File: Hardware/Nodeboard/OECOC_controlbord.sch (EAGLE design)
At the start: 13 parts, among them IC1 DS2405, IC2 DS2405, U1 ESP32-DEVKITC-32D

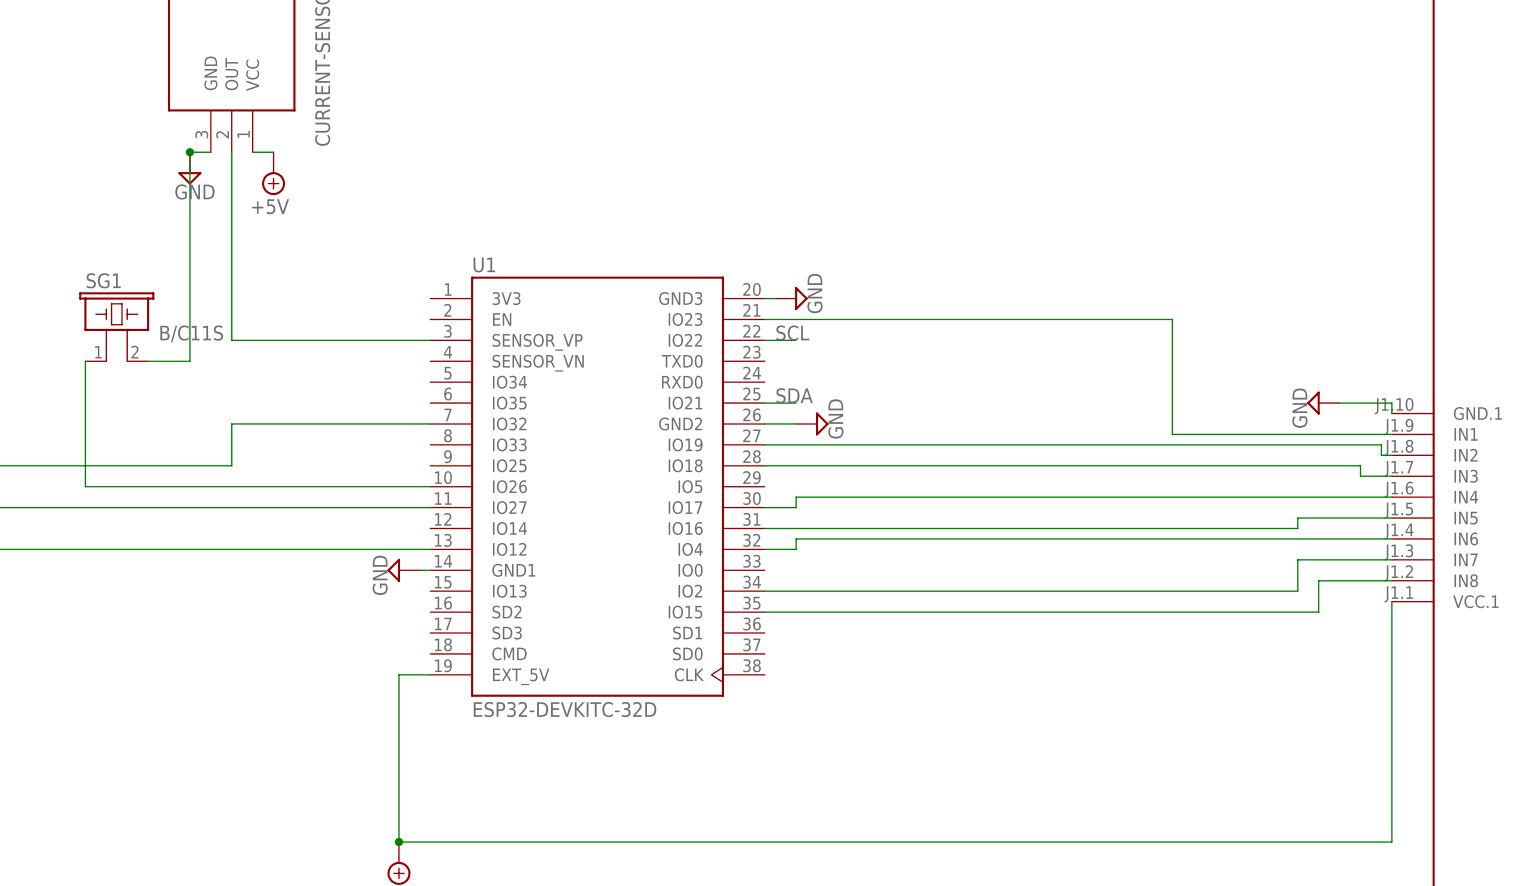
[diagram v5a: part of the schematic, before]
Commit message: changed pins relay
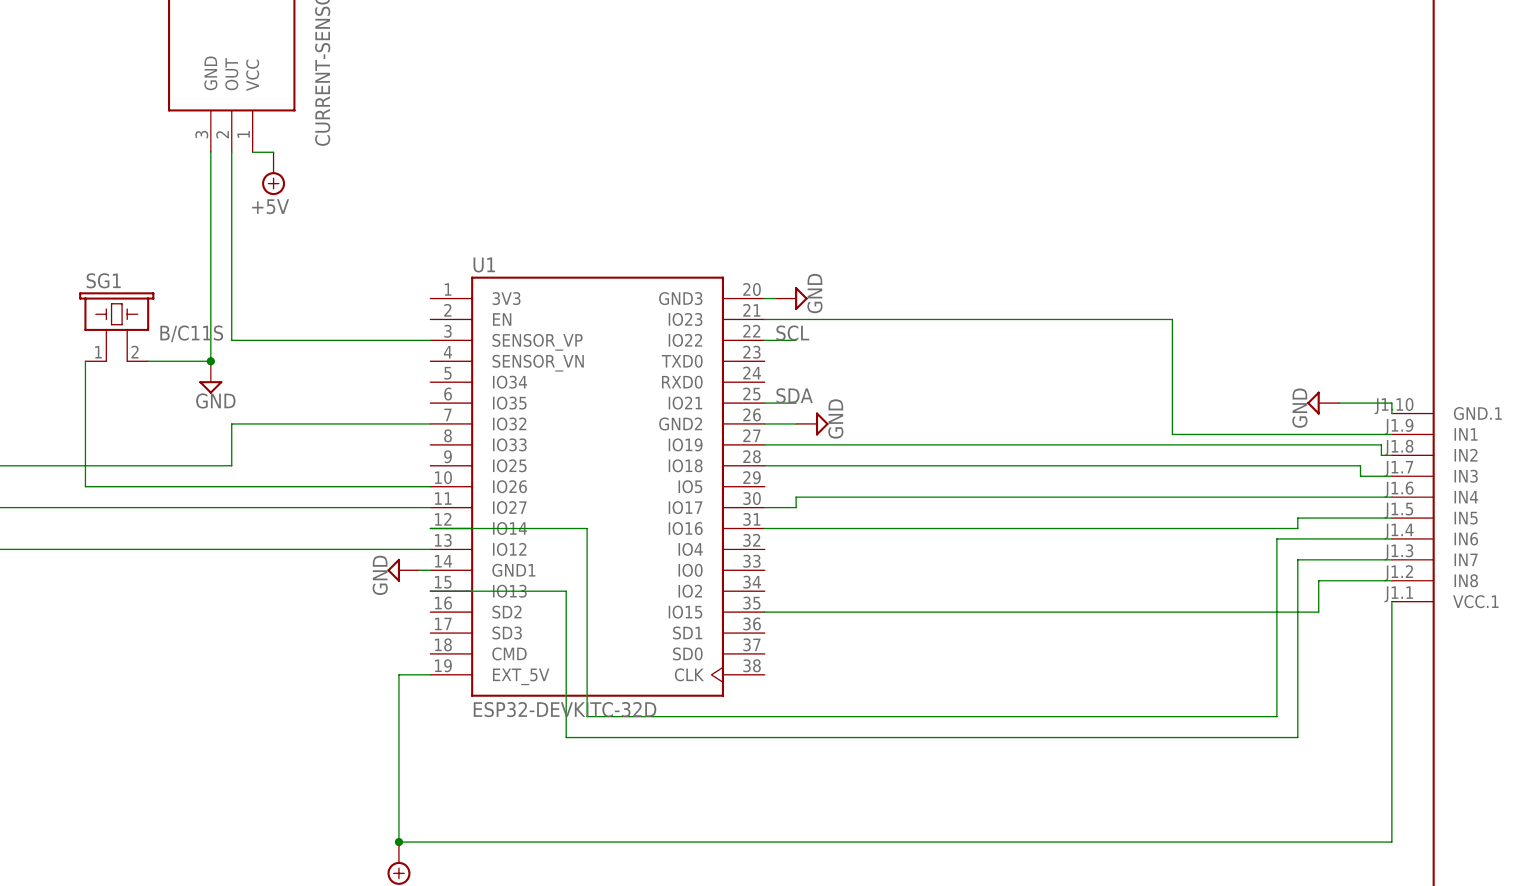
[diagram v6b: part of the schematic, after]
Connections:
- net N$2: now also U1.IO14; no longer U1.IO4
- net N$7: now also U1.IO13; no longer U1.IO2
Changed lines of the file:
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@@
 <attribute name="VALUE" x="194.945" y="210.185" size="1.778" layer="96" rot="R180"/>
 </instance>
-<instance part="G5" gate="G$1" x="182.88" y="213.36" smashed="yes">
-<attribute name="VALUE" x="180.975" y="210.185" size="1.778" layer="96"/>
+<instance part="G5" gate="G$1" x="185.42" y="187.96" smashed="yes">
+<attribute name="VALUE" x="183.515" y="184.785" size="1.778" layer="96"/>
 </instance>
 <instance part="U$5" gate="G$1" x="91.44" y="116.84" smashed="yes" rot="R180">
@@
 <pinref part="G5" gate="G$1" pin="GND"/>
 <pinref part="U$4" gate="G$1" pin="GND"/>
-<wire x1="182.88" y1="215.9" x2="185.42" y2="215.9" width="0.1524" layer="91"/>
+<wire x1="185.42" y1="190.5" x2="185.42" y2="215.9" width="0.1524" layer="91"/>
 <pinref part="SG1" gate="G$1" pin="2"/>
-<wire x1="177.8" y1="190.5" x2="182.88" y2="190.5" width="0.1524" layer="91"/>
-<wire x1="182.88" y1="190.5" x2="182.88" y2="215.9" width="0.1524" layer="91"/>
-<junction x="182.88" y="215.9"/>
+<wire x1="177.8" y1="190.5" x2="185.42" y2="190.5" width="0.1524" layer="91"/>
+<junction x="185.42" y="190.5"/>
 </segment>
 <segment>
@@
 </segment>
 </net>
-<net name="N$2" class="0">
-<segment>
-<pinref part="U1" gate="G$1" pin="IO4"/>
-<wire x1="252.73" y1="167.64" x2="256.54" y2="167.64" width="0.1524" layer="91"/>
-<pinref part="U$1" gate="G$1" pin="IN6"/>
-<wire x1="256.54" y1="167.64" x2="256.54" y2="168.91" width="0.1524" layer="91"/>
-<wire x1="256.54" y1="168.91" x2="328.93" y2="168.91" width="0.1524" layer="91"/>
-</segment>
-</net>
 <net name="N$3" class="0">
 <segment>
@@
 <net name="N$7" class="0">
 <segment>
-<pinref part="U1" gate="G$1" pin="IO2"/>
-<wire x1="252.73" y1="162.56" x2="317.5" y2="162.56" width="0.1524" layer="91"/>
 <pinref part="U$1" gate="G$1" pin="IN7"/>
-<wire x1="317.5" y1="162.56" x2="317.5" y2="166.37" width="0.1524" layer="91"/>
 <wire x1="317.5" y1="166.37" x2="328.93" y2="166.37" width="0.1524" layer="91"/>
+<wire x1="317.5" y1="166.37" x2="317.5" y2="144.78" width="0.1524" layer="91"/>
+<wire x1="317.5" y1="144.78" x2="228.6" y2="144.78" width="0.1524" layer="91"/>
+<wire x1="228.6" y1="144.78" x2="228.6" y2="162.56" width="0.1524" layer="91"/>
+<pinref part="U1" gate="G$1" pin="IO13"/>
+<wire x1="228.6" y1="162.56" x2="212.09" y2="162.56" width="0.1524" layer="91"/>
 </segment>
 </net>
@@
 </segment>
 </net>
+<net name="N$2" class="0">
+<segment>
+<pinref part="U$1" gate="G$1" pin="IN6"/>
+<wire x1="328.93" y1="168.91" x2="314.96" y2="168.91" width="0.1524" layer="91"/>
+<wire x1="314.96" y1="168.91" x2="314.96" y2="147.32" width="0.1524" layer="91"/>
+<wire x1="314.96" y1="147.32" x2="231.14" y2="147.32" width="0.1524" layer="91"/>
+<wire x1="231.14" y1="147.32" x2="231.14" y2="170.18" width="0.1524" layer="91"/>
+<pinref part="U1" gate="G$1" pin="IO14"/>
+<wire x1="231.14" y1="170.18" x2="212.09" y2="170.18" width="0.1524" layer="91"/>
+</segment>
+</net>

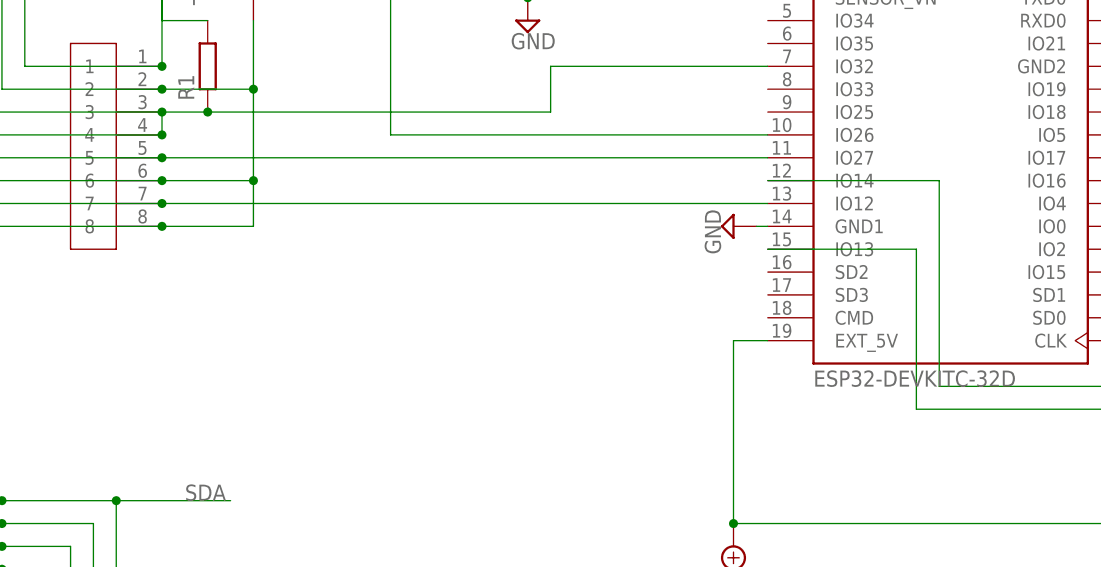
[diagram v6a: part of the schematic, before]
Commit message: changed pin relay and reeds
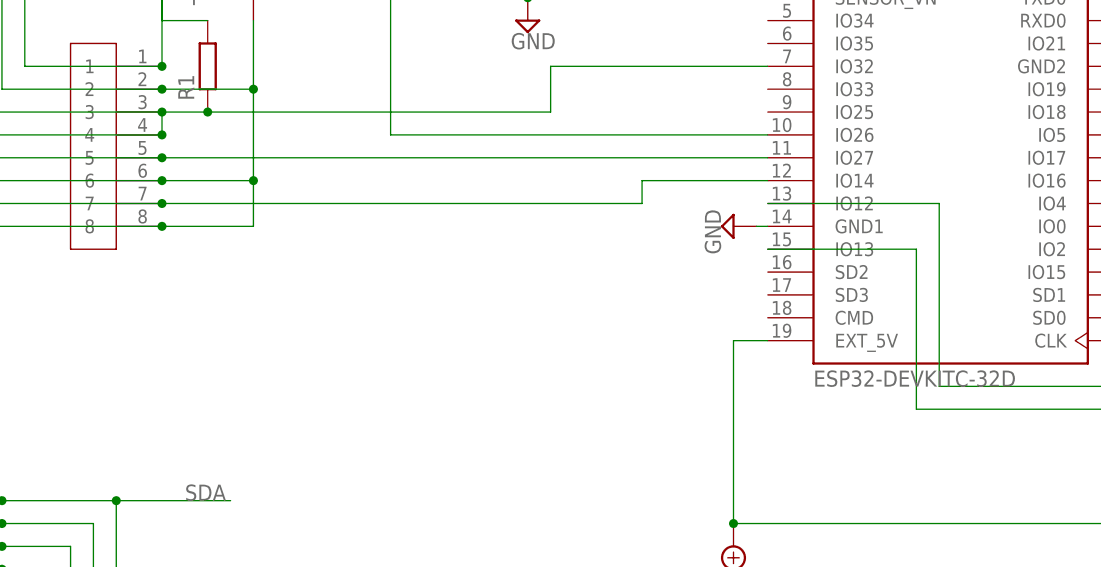
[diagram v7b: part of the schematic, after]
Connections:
- net N$14: now also U1.IO14; no longer U1.IO12
- net N$2: now also U1.IO12; no longer U1.IO14
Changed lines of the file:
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@@
 <pinref part="U$6" gate="G$1" pin="7"/>
 <wire x1="88.9" y1="167.64" x2="144.78" y2="167.64" width="0.1524" layer="91"/>
-<pinref part="U1" gate="G$1" pin="IO12"/>
-<wire x1="144.78" y1="167.64" x2="212.09" y2="167.64" width="0.1524" layer="91"/>
+<wire x1="144.78" y1="167.64" x2="198.12" y2="167.64" width="0.1524" layer="91"/>
 <junction x="144.78" y="167.64"/>
+<wire x1="198.12" y1="167.64" x2="198.12" y2="170.18" width="0.1524" layer="91"/>
+<pinref part="U1" gate="G$1" pin="IO14"/>
+<wire x1="198.12" y1="170.18" x2="212.09" y2="170.18" width="0.1524" layer="91"/>
 </segment>
 </net>
@@
 <wire x1="314.96" y1="168.91" x2="314.96" y2="147.32" width="0.1524" layer="91"/>
 <wire x1="314.96" y1="147.32" x2="231.14" y2="147.32" width="0.1524" layer="91"/>
-<wire x1="231.14" y1="147.32" x2="231.14" y2="170.18" width="0.1524" layer="91"/>
-<pinref part="U1" gate="G$1" pin="IO14"/>
-<wire x1="231.14" y1="170.18" x2="212.09" y2="170.18" width="0.1524" layer="91"/>
+<wire x1="231.14" y1="147.32" x2="231.14" y2="167.64" width="0.1524" layer="91"/>
+<pinref part="U1" gate="G$1" pin="IO12"/>
+<wire x1="231.14" y1="167.64" x2="212.09" y2="167.64" width="0.1524" layer="91"/>
 </segment>
 </net>

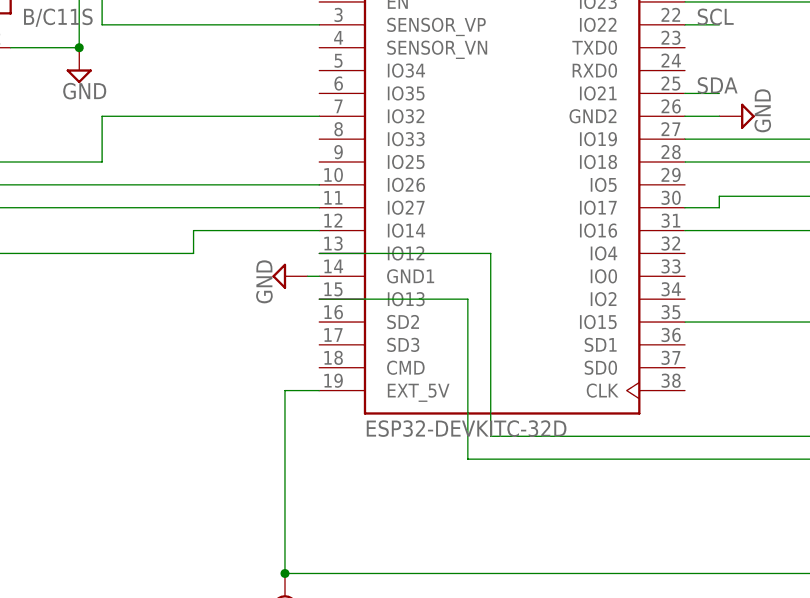
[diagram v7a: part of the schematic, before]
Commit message: edit pins relay
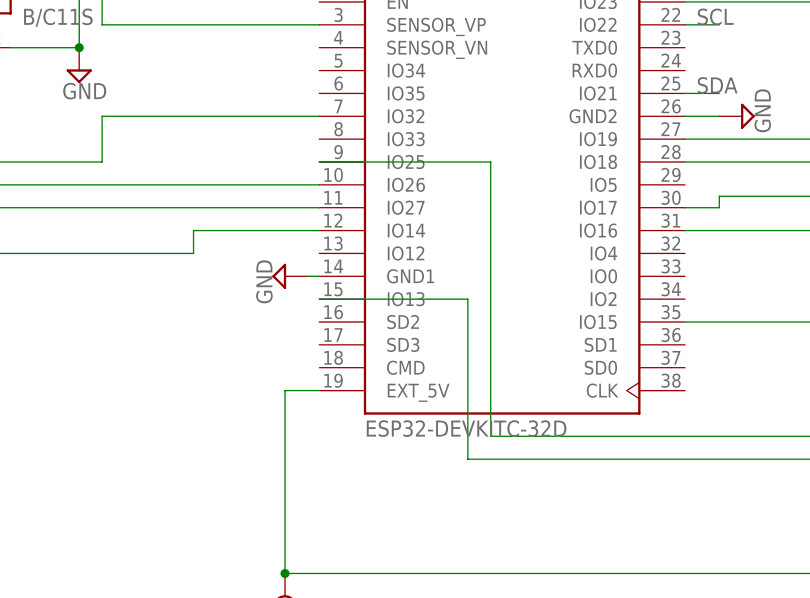
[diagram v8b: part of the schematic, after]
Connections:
- net N$2: now also U1.IO25; no longer U1.IO12
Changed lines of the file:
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@@
 <wire x1="314.96" y1="168.91" x2="314.96" y2="147.32" width="0.1524" layer="91"/>
 <wire x1="314.96" y1="147.32" x2="231.14" y2="147.32" width="0.1524" layer="91"/>
-<wire x1="231.14" y1="147.32" x2="231.14" y2="167.64" width="0.1524" layer="91"/>
-<pinref part="U1" gate="G$1" pin="IO12"/>
-<wire x1="231.14" y1="167.64" x2="212.09" y2="167.64" width="0.1524" layer="91"/>
+<wire x1="231.14" y1="147.32" x2="231.14" y2="177.8" width="0.1524" layer="91"/>
+<pinref part="U1" gate="G$1" pin="IO25"/>
+<wire x1="231.14" y1="177.8" x2="212.09" y2="177.8" width="0.1524" layer="91"/>
 </segment>
 </net>
